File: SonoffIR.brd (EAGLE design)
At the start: 12.9 x 12.6 mm, 5 parts, among them Q1 2N2222

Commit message: Better Name/Value placement on Board
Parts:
- R1: value 2.5 Ohm -> 2.5
- RB: value 2.7k Ohm -> 2.7k
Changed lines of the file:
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@@
 <layer number="27" name="tValues" color="7" fill="1" visible="yes" active="yes"/>
 <layer number="28" name="bValues" color="7" fill="1" visible="yes" active="yes"/>
-<layer number="29" name="tStop" color="7" fill="3" visible="no" active="yes"/>
-<layer number="30" name="bStop" color="7" fill="6" visible="no" active="yes"/>
+<layer number="29" name="tStop" color="7" fill="3" visible="yes" active="yes"/>
+<layer number="30" name="bStop" color="7" fill="6" visible="yes" active="yes"/>
 <layer number="31" name="tCream" color="7" fill="4" visible="no" active="yes"/>
 <layer number="32" name="bCream" color="7" fill="5" visible="no" active="yes"/>
@@
 <elements>
 <element name="D1" library="led" package="SFH482" value="IR LED" x="6.35" y="5.08" rot="R90"/>
-<element name="Q1" library="transistor-npn" package="TO92" value="2N2222" x="10.16" y="9.525" rot="MR0"/>
-<element name="R1" library="resistor" package="0204V" value="2.5 Ohm" x="5.08" y="1.27" rot="MR180"/>
-<element name="RB" library="resistor" package="0204V" value="2.7k Ohm" x="5.08" y="11.43" rot="MR0"/>
-<element name="SV1" library="con-lsta" package="FE05-1" value="" x="1.27" y="6.35" rot="MR90">
+<element name="Q1" library="transistor-npn" package="TO92" value="2N2222" x="10.16" y="9.525" smashed="yes" rot="MR0">
+<attribute name="NAME" x="17.145" y="12.7" size="1.27" layer="26" ratio="10" rot="MR0"/>
+<attribute name="VALUE" x="12.573" y="7.493" size="1.27" layer="28" ratio="10" rot="MR270"/>
+</element>
+<element name="R1" library="resistor" package="0204V" value="2.5" x="5.08" y="1.27" smashed="yes" rot="MR180">
+<attribute name="NAME" x="4.2164" y="-0.4064" size="1.27" layer="26" ratio="10" rot="MR180"/>
+<attribute name="VALUE" x="7.2644" y="1.5494" size="1.27" layer="28" ratio="10" rot="MR180"/>
+</element>
+<element name="RB" library="resistor" package="0204V" value="2.7k" x="5.08" y="11.43" smashed="yes" rot="MR0">
+<attribute name="NAME" x="6.1976" y="12.8524" size="1.27" layer="26" ratio="10" rot="MR0"/>
+<attribute name="VALUE" x="5.9436" y="9.3726" size="1.27" layer="28" ratio="10" rot="MR0"/>
+</element>
+<element name="SV1" library="con-lsta" package="FE05-1" value="" x="1.27" y="6.35" smashed="yes" rot="MR90">
 <attribute name="OC_NEWARK" value="unknown" x="1.27" y="6.35" size="1.778" layer="28" rot="MR90" display="off"/>
 <attribute name="MF" value="" x="1.27" y="6.35" size="1.778" layer="28" rot="MR90" display="off"/>
 <attribute name="OC_FARNELL" value="unknown" x="1.27" y="6.35" size="1.778" layer="28" rot="MR90" display="off"/>
 <attribute name="MPN" value="" x="1.27" y="6.35" size="1.778" layer="28" rot="MR90" display="off"/>
+<attribute name="NAME" x="-7.239" y="7.62" size="1.27" layer="26" ratio="10" rot="MR90"/>
+<attribute name="VALUE" x="2.921" y="6.35" size="1.27" layer="28" ratio="10" rot="MR90"/>
 </element>
 </elements>

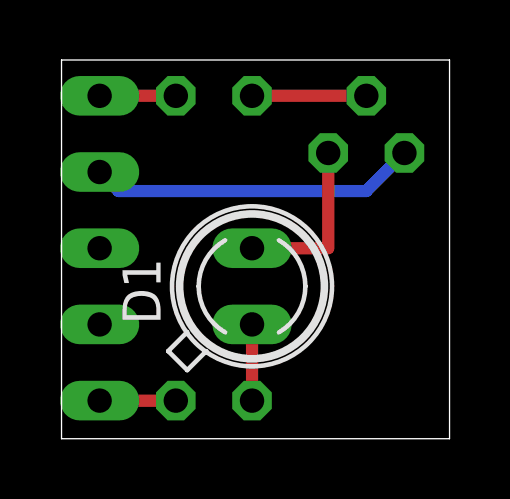
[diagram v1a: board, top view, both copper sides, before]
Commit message: Changes in Value placement
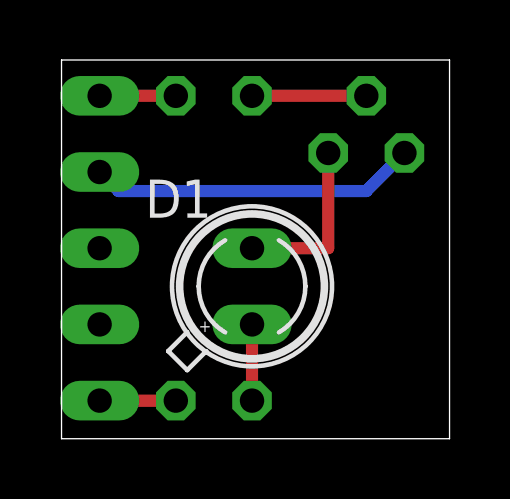
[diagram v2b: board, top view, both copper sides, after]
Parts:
- 2.5: value 2.5 -> (none)
- 2.7K: value 2.7k -> (none)
- 2N2222: value 2N2222 -> (none)
- renumbered Q1 to 2N2222, R1 to 2.5, RB to 2.7K
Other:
- board text added: "+"
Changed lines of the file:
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@@
 <wire x1="12.934" y1="12.624" x2="0" y2="12.624" width="0" layer="20"/>
 <wire x1="0" y1="12.624" x2="0" y2="0" width="0" layer="20"/>
+<text x="4.572" y="3.556" size="0.4064" layer="25">+</text>
 </plain>
 <attributes>
@@
 </autorouter>
 <elements>
-<element name="D1" library="led" package="SFH482" value="IR LED" x="6.35" y="5.08" rot="R90"/>
-<element name="Q1" library="transistor-npn" package="TO92" value="2N2222" x="10.16" y="9.525" smashed="yes" rot="MR0">
-<attribute name="NAME" x="17.145" y="12.7" size="1.27" layer="26" ratio="10" rot="MR0"/>
+<element name="D1" library="led" package="SFH482" value="IR LED" x="6.35" y="5.08" smashed="yes" rot="R90">
+<attribute name="NAME" x="2.794" y="7.366" size="1.27" layer="25" ratio="10"/>
+<attribute name="VALUE" x="10.668" y="2.032" size="1.27" layer="27" ratio="10" rot="R90"/>
+</element>
+<element name="2N2222" library="transistor-npn" package="TO92" value="" x="10.16" y="9.525" smashed="yes" rot="MR0">
+<attribute name="NAME" x="12.7" y="7.747" size="1.27" layer="26" ratio="10" rot="MR270"/>
 <attribute name="VALUE" x="12.573" y="7.493" size="1.27" layer="28" ratio="10" rot="MR270"/>
 </element>
-<element name="R1" library="resistor" package="0204V" value="2.5" x="5.08" y="1.27" smashed="yes" rot="MR180">
-<attribute name="NAME" x="4.2164" y="-0.4064" size="1.27" layer="26" ratio="10" rot="MR180"/>
+<element name="2.5" library="resistor" package="0204V" value="" x="5.08" y="1.27" smashed="yes" rot="MR180">
+<attribute name="NAME" x="7.5184" y="1.8796" size="1.27" layer="26" ratio="10" rot="MR180"/>
 <attribute name="VALUE" x="7.2644" y="1.5494" size="1.27" layer="28" ratio="10" rot="MR180"/>
 </element>
-<element name="RB" library="resistor" package="0204V" value="2.7k" x="5.08" y="11.43" smashed="yes" rot="MR0">
-<attribute name="NAME" x="6.1976" y="12.8524" size="1.27" layer="26" ratio="10" rot="MR0"/>
-<attribute name="VALUE" x="5.9436" y="9.3726" size="1.27" layer="28" ratio="10" rot="MR0"/>
+<element name="2.7K" library="resistor" package="0204V" value="" x="5.08" y="11.43" smashed="yes" rot="MR0">
+<attribute name="NAME" x="6.7056" y="8.7884" size="1.27" layer="26" ratio="10" rot="MR0"/>
+<attribute name="VALUE" x="6.7056" y="8.8646" size="1.27" layer="28" ratio="10" rot="MR0"/>
 </element>
 <element name="SV1" library="con-lsta" package="FE05-1" value="" x="1.27" y="6.35" smashed="yes" rot="MR90">
@@
 <attribute name="OC_FARNELL" value="unknown" x="1.27" y="6.35" size="1.778" layer="28" rot="MR90" display="off"/>
 <attribute name="MPN" value="" x="1.27" y="6.35" size="1.778" layer="28" rot="MR90" display="off"/>
-<attribute name="NAME" x="-7.239" y="7.62" size="1.27" layer="26" ratio="10" rot="MR90"/>
+<attribute name="NAME" x="2.667" y="3.81" size="1.27" layer="26" ratio="10" rot="MR90"/>
 <attribute name="VALUE" x="2.921" y="6.35" size="1.27" layer="28" ratio="10" rot="MR90"/>
 </element>
@@
 <signal name="GPIO14">
 <contactref element="SV1" pad="5"/>
-<contactref element="RB" pad="2"/>
+<contactref element="2.7K" pad="2"/>
 <wire x1="1.27" y1="11.43" x2="3.81" y2="11.43" width="0.4064" layer="1"/>
 </signal>
 <signal name="3V3">
 <contactref element="SV1" pad="1"/>
-<contactref element="R1" pad="1"/>
+<contactref element="2.5" pad="1"/>
 <wire x1="1.27" y1="1.27" x2="3.81" y2="1.27" width="0.4064" layer="1"/>
 </signal>
 <signal name="GND">
 <contactref element="SV1" pad="4"/>
-<contactref element="Q1" pad="3"/>
+<contactref element="2N2222" pad="3"/>
 <wire x1="1.27" y1="8.89" x2="1.905" y2="8.255" width="0.4064" layer="16"/>
 <wire x1="1.905" y1="8.255" x2="10.16" y2="8.255" width="0.4064" layer="16"/>
@@
 </signal>
 <signal name="N$1">
-<contactref element="R1" pad="2"/>
+<contactref element="2.5" pad="2"/>
 <contactref element="D1" pad="A"/>
 <wire x1="6.35" y1="1.27" x2="6.35" y2="3.81" width="0.4064" layer="1"/>
 </signal>
 <signal name="N$2">
-<contactref element="RB" pad="1"/>
-<contactref element="Q1" pad="2"/>
+<contactref element="2.7K" pad="1"/>
+<contactref element="2N2222" pad="2"/>
 <wire x1="6.35" y1="11.43" x2="10.16" y2="11.43" width="0.4064" layer="1"/>
 </signal>
 <signal name="N$3">
 <contactref element="D1" pad="K"/>
-<contactref element="Q1" pad="1"/>
+<contactref element="2N2222" pad="1"/>
 <wire x1="6.35" y1="6.35" x2="8.89" y2="6.35" width="0.4064" layer="1"/>
 <wire x1="8.89" y1="6.35" x2="8.89" y2="9.525" width="0.4064" layer="1"/>
